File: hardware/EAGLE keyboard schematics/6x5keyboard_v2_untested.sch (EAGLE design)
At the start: 71 parts

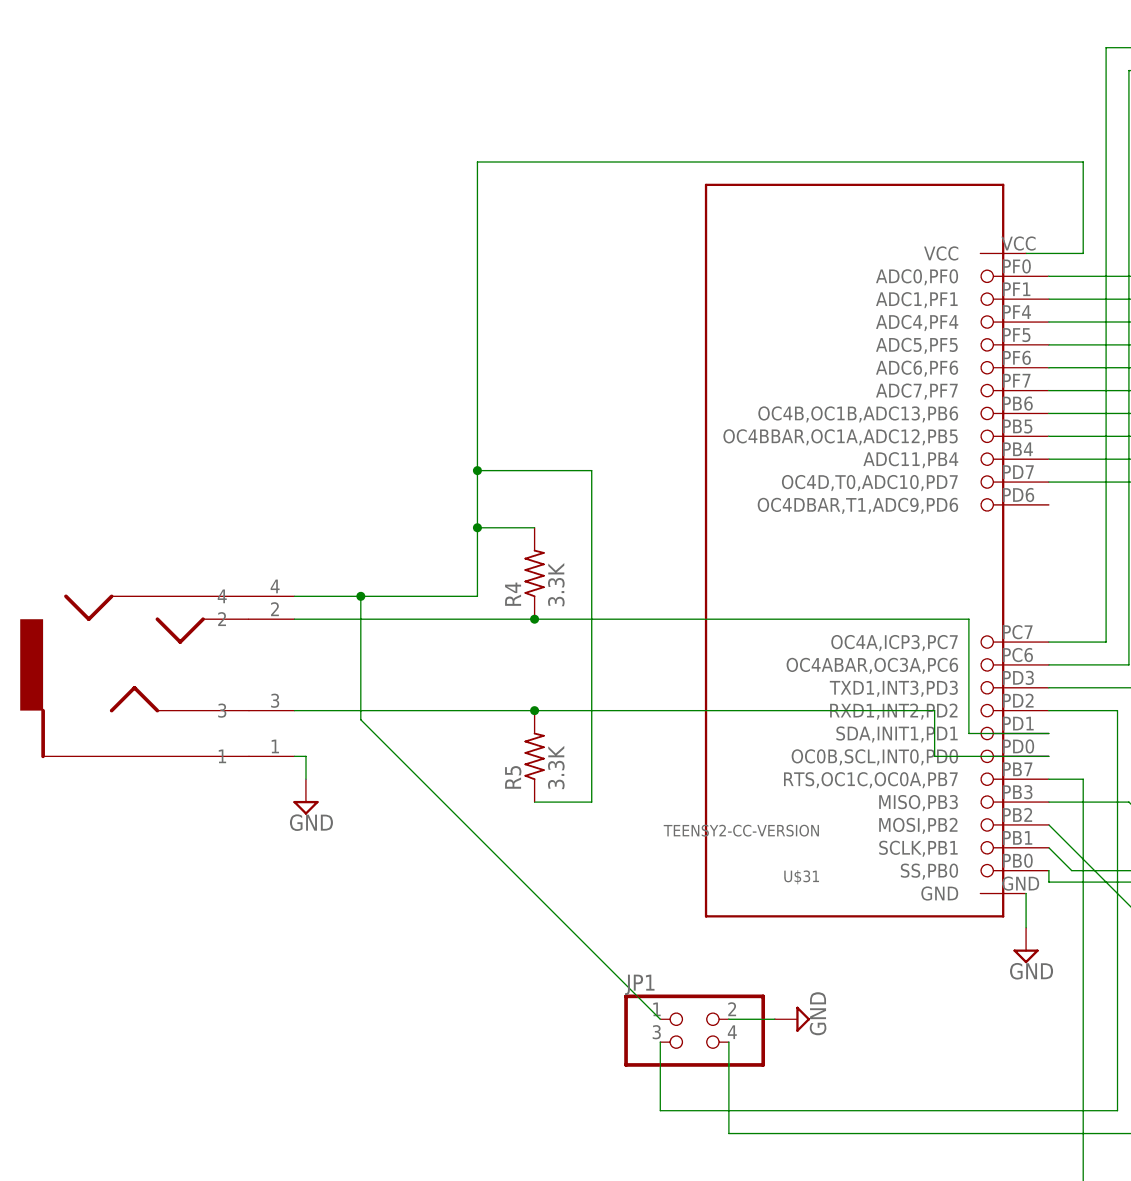
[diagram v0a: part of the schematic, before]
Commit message: Replaced TRRS connector with dual USB-A connector
Added dual USB-A connector to allow for better daisy-chaining support
(including possible support for hot-swapping). Thanks to CaitSith2 for
assistance.
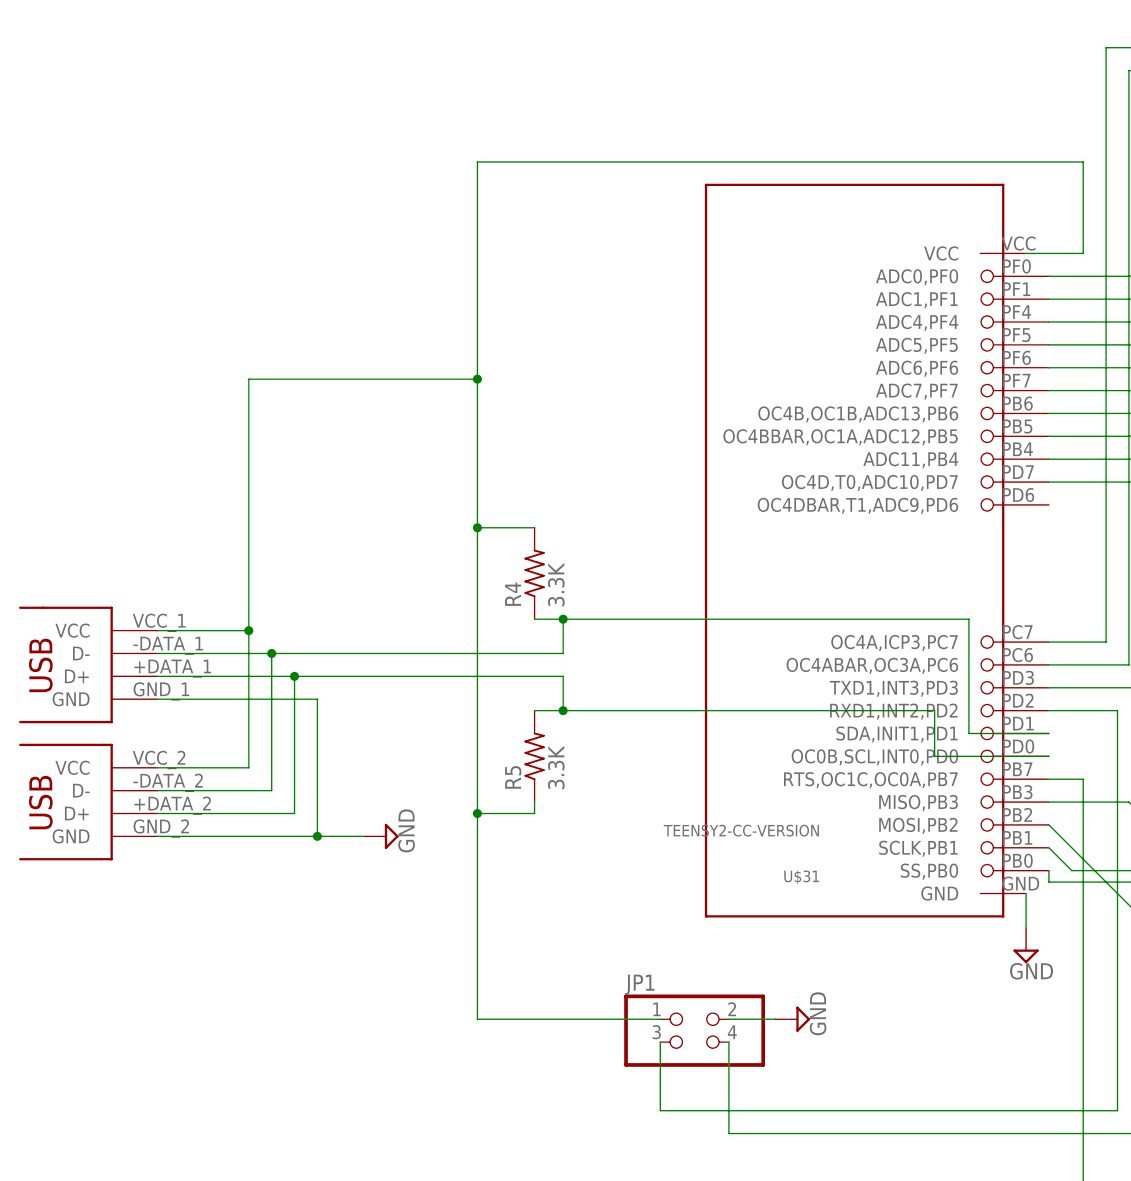
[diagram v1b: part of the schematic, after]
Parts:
- removed COMM: SJ-43514_HEADPHONES_3.5MM_X4, my_parts:SJ-43514_HEADPHONES_3.5MM_X4
- added U$35: DUAL-USB-A, my_parts:DUAL-USB-A
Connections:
- removed net N$52: COMM.3, R5.2, U$31.OC0B,SCL,INT0,PD0
- removed net N$53: COMM.2, R4.1, U$31.SDA,INIT1,PD1
- new net N$57: R4.1, U$31.SDA,INIT1,PD1, U$35G$1.D-, U$35G$2.D-
- new net N$58: R5.2, U$31.OC0B,SCL,INT0,PD0, U$35G$1.D+, U$35G$2.D+
- net GND: now also U$35G$1.GND, U$35G$2.GND; no longer COMM.1
- net N$51: now also U$35G$1.VCC, U$35G$2.VCC; no longer COMM.4
